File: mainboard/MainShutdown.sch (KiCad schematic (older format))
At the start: 41 parts, among them J5 AIR-, J6 AIR+, K1 KT12-1A, K2 UMS05-1A80-75L, Q1 TSM2306, Q14 BC846AW, Q17 DMN10H220L-7, Q18 TSM2306, Q19 TSM2306, Q20 TSM2306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

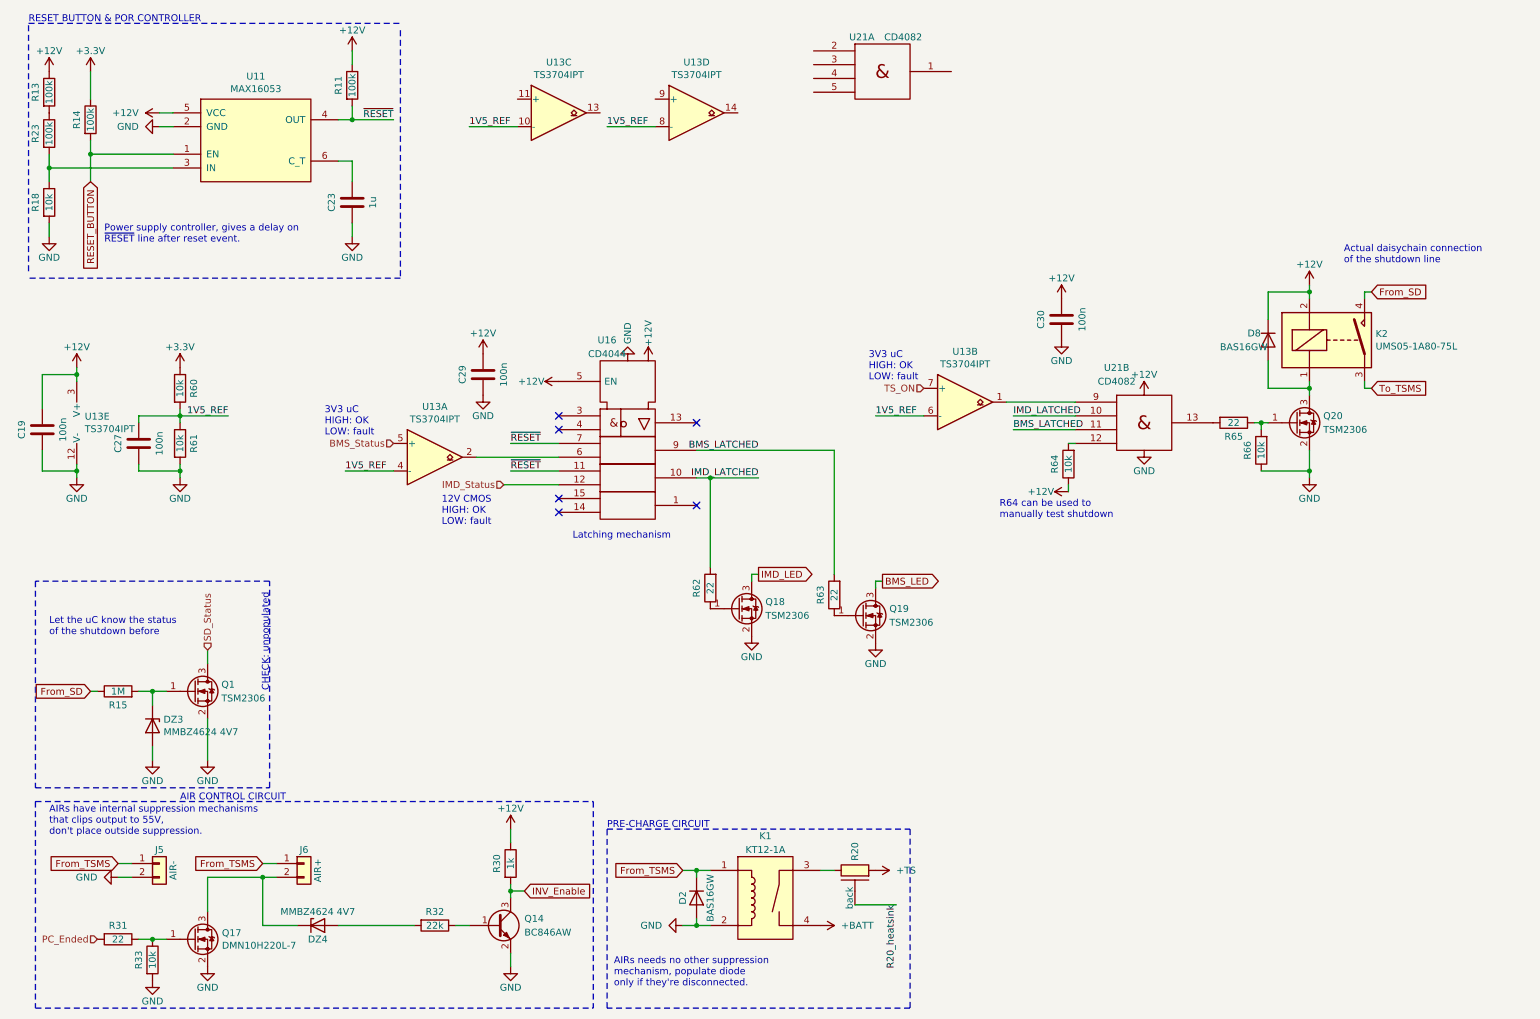
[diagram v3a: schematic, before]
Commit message: corrected pulldown and air+ mosfet driving
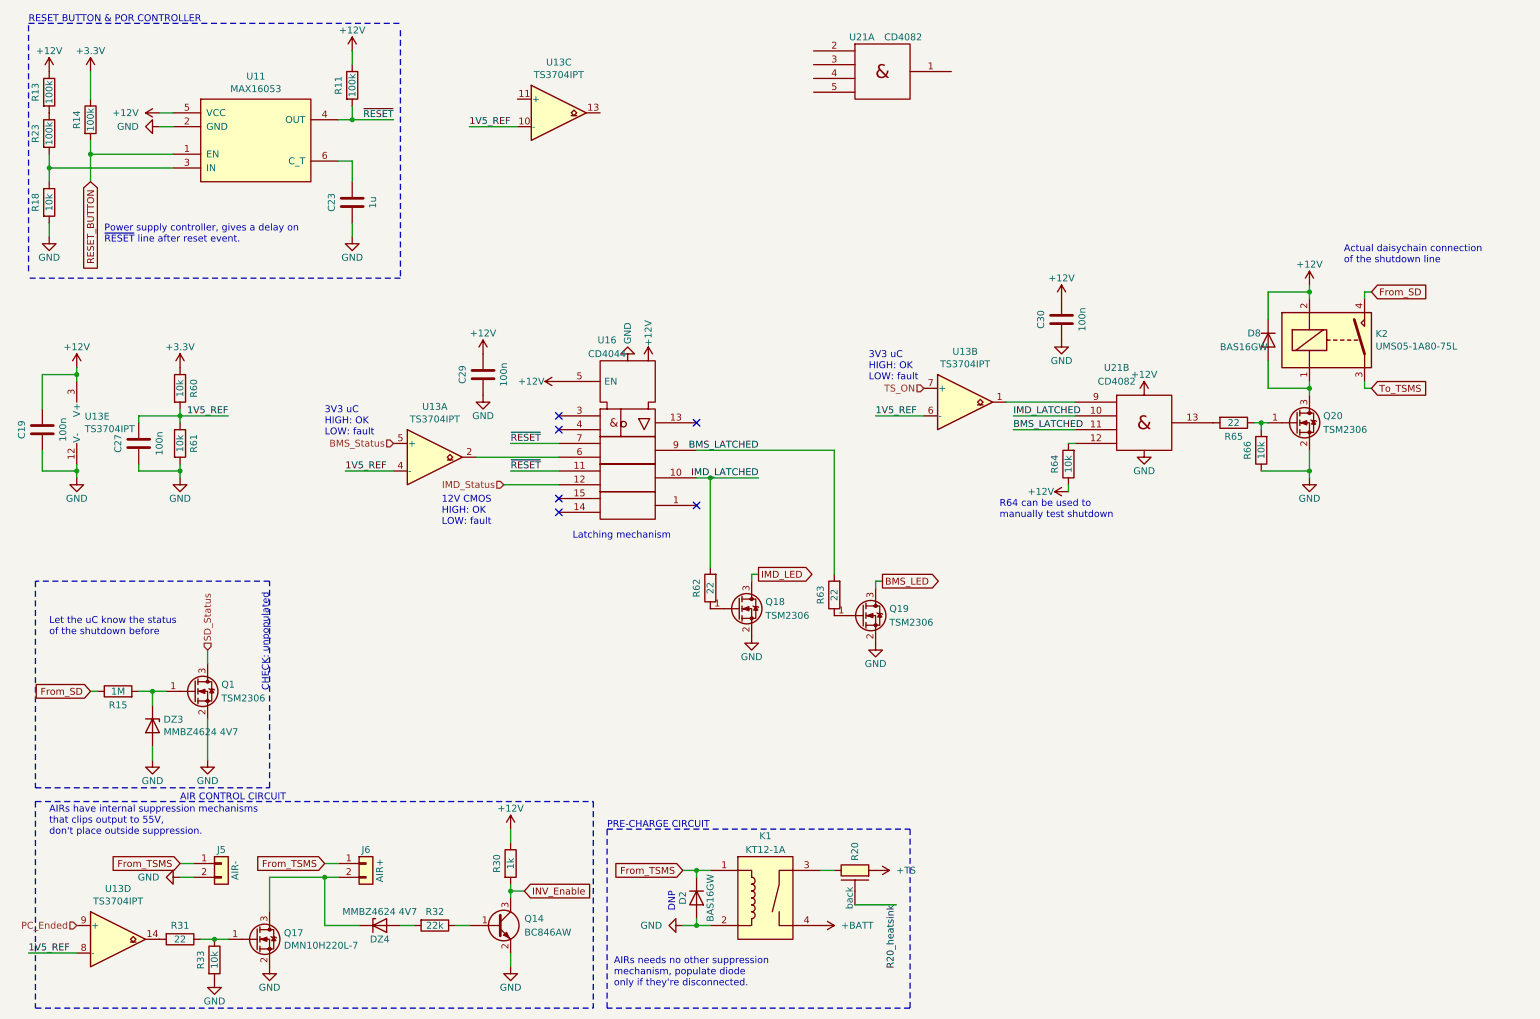
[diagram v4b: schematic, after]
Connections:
- net PC_Ended: now also U13.9 (+); no longer R31.2
- net at U13.14: now also R31.2
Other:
- note added: "DNP"
- moved on the sheet: DZ4, J5, J6, Q17, R31, R33, U13D
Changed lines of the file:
@@
 L Connector_Generic:Conn_01x02 J6
 U 1 1 5B0DE10C
-P 2550 6700
-F 0 "J6" H 2550 6800 50  0000 C CNN
-F 1 "AIR+" V 2650 6650 50  0000 C CNN
-F 2 "Connector_Molex:Molex_Micro-Fit_3.0_43650-0215_1x02_P3.00mm_Vertical" H 2550 6700 50  0001 C CNN
-F 3 "http://www.gigavac.com/sites/default/files/catalog/spec_sheet/gx14.pdf" H 2550 6700 50  0001 C CNN
-	1    2550 6700
+P 3000 6700
+F 0 "J6" H 3000 6800 50  0000 C CNN
+F 1 "AIR+" V 3100 6650 50  0000 C CNN
+F 2 "Connector_Molex:Molex_Micro-Fit_3.0_43650-0215_1x02_P3.00mm_Vertical" H 3000 6700 50  0001 C CNN
+F 3 "http://www.gigavac.com/sites/default/files/catalog/spec_sheet/gx14.pdf" H 3000 6700 50  0001 C CNN
+	1    3000 6700
 	1    0    0    -1
 $EndComp
@@
 L Device:R R33
 U 1 1 5B0DE119
-P 1450 7400
-F 0 "R33" V 1350 7400 50  0000 C CNN
-F 1 "10k" V 1450 7400 50  0000 C CNN
-F 2 "Resistor_SMD:R_0805_2012Metric" V 1380 7400 50  0001 C CNN
-F 3 "~" H 1450 7400 50  0001 C CNN
-	1    1450 7400
+P 1900 7400
+F 0 "R33" V 1800 7400 50  0000 C CNN
+F 1 "10k" V 1900 7400 50  0000 C CNN
+F 2 "Resistor_SMD:R_0805_2012Metric" V 1830 7400 50  0001 C CNN
+F 3 "~" H 1900 7400 50  0001 C CNN
+	1    1900 7400
 	1    0    0    -1
 $EndComp
@@
 L power:GND #PWR094
 U 1 1 5B0DE121
-P 1450 7550
-F 0 "#PWR094" H 1450 7300 50  0001 C CNN
-F 1 "GND" H 1450 7400 50  0000 C CNN
-F 2 "" H 1450 7550 50  0001 C CNN
-F 3 "" H 1450 7550 50  0001 C CNN
-	1    1450 7550
+P 1900 7550
+F 0 "#PWR094" H 1900 7300 50  0001 C CNN
+F 1 "GND" H 1900 7400 50  0000 C CNN
+F 2 "" H 1900 7550 50  0001 C CNN
+F 3 "" H 1900 7550 50  0001 C CNN
+	1    1900 7550
 	1    0    0    -1
 $EndComp
@@
 L Device:R R31
 U 1 1 5B0DE127
-P 1200 7250
-F 0 "R31" V 1100 7250 50  0000 C CNN
-F 1 "22" V 1200 7250 50  0000 C CNN
-F 2 "Resistor_SMD:R_0805_2012Metric" V 1130 7250 50  0001 C CNN
-F 3 "~" H 1200 7250 50  0001 C CNN
-	1    1200 7250
+P 1650 7250
+F 0 "R31" V 1550 7250 50  0000 C CNN
+F 1 "22" V 1650 7250 50  0000 C CNN
+F 2 "Resistor_SMD:R_0805_2012Metric" V 1580 7250 50  0001 C CNN
+F 3 "~" H 1650 7250 50  0001 C CNN
+	1    1650 7250
 	0    1    1    0
 $EndComp
@@
 L Device:D_Zener DZ4
 U 1 1 5B0DE15E
-P 2650 7150
-F 0 "DZ4" H 2650 7050 50  0000 C CNN
-F 1 "MMBZ4624 4V7" H 2650 7250 50  0000 C CNN
-F 2 "Diode_SMD:D_SOT-23_ANK" H 2650 7150 50  0001 C CNN
-F 3 "http://www.vishay.com/docs/85770/mmbz4617.pdf" H 2650 7150 50  0001 C CNN
-	1    2650 7150
+P 3100 7150
+F 0 "DZ4" H 3100 7050 50  0000 C CNN
+F 1 "MMBZ4624 4V7" H 3100 7250 50  0000 C CNN
+F 2 "Diode_SMD:D_SOT-23_ANK" H 3100 7150 50  0001 C CNN
+F 3 "http://www.vishay.com/docs/85770/mmbz4617.pdf" H 3100 7150 50  0001 C CNN
+	1    3100 7150
 	1    0    0    -1
 $EndComp
@@
 L Connector_Generic:Conn_01x02 J5
 U 1 1 5B0DE167
-P 1500 6700
-F 0 "J5" H 1500 6800 50  0000 C CNN
-F 1 "AIR-" V 1600 6650 50  0000 C CNN
-F 2 "Connector_Molex:Molex_Micro-Fit_3.0_43650-0215_1x02_P3.00mm_Vertical" H 1500 6700 50  0001 C CNN
-F 3 "http://www.gigavac.com/sites/default/files/catalog/spec_sheet/gx14.pdf" H 1500 6700 50  0001 C CNN
-	1    1500 6700
+P 1950 6700
+F 0 "J5" H 1950 6800 50  0000 C CNN
+F 1 "AIR-" V 2050 6650 50  0000 C CNN
+F 2 "Connector_Molex:Molex_Micro-Fit_3.0_43650-0215_1x02_P3.00mm_Vertical" H 1950 6700 50  0001 C CNN
+F 3 "http://www.gigavac.com/sites/default/files/catalog/spec_sheet/gx14.pdf" H 1950 6700 50  0001 C CNN
+	1    1950 6700
 	1    0    0    -1
 $EndComp
@@
 L power:GND #PWR091
 U 1 1 5B0DE170
-P 1200 6800
-F 0 "#PWR091" H 1200 6550 50  0001 C CNN
-F 1 "GND" V 1200 6650 50  0000 R CNN
-F 2 "" H 1200 6800 50  0001 C CNN
-F 3 "" H 1200 6800 50  0001 C CNN
-	1    1200 6800
+P 1650 6800
+F 0 "#PWR091" H 1650 6550 50  0001 C CNN
+F 1 "GND" V 1650 6650 50  0000 R CNN
+F 2 "" H 1650 6800 50  0001 C CNN
+F 3 "" H 1650 6800 50  0001 C CNN
+	1    1650 6800
 	0    1    1    0
 $EndComp
@@
 Wire Wire Line
 	5400 6750 5500 6750
-Text HLabel 1050 7250 0    50   Input ~ 0
+Text HLabel 900  7150 0    50   Input ~ 0
 PC_Ended
 Wire Wire Line
@@
 INV_Enable
 Wire Wire Line
-	2350 6700 2250 6700
-Text GLabel 2250 6700 0    50   Input ~ 0
+	2800 6700 2700 6700
+Text GLabel 2700 6700 0    50   Input ~ 0
 From_TSMS
 Wire Wire Line
-	1200 6800 1300 6800
-Wire Wire Line
-	1300 6700 1200 6700
-Text GLabel 1200 6700 0    50   Input ~ 0
+	1650 6800 1750 6800
+Wire Wire Line
+	1750 6700 1650 6700
+Text GLabel 1650 6700 0    50   Input ~ 0
 From_TSMS
 Wire Wire Line
@@
 L Device:Q_NMOS_GSD Q17
 U 1 1 6041C6DC
-P 1750 7250
-F 0 "Q17" H 1954 7296 50  0000 L CNN
-F 1 "DMN10H220L-7 " H 1954 7205 50  0000 L CNN
-F 2 "Package_TO_SOT_SMD:SOT-23" H 1950 7350 50  0001 C CNN
-F 3 "https://www.mouser.it/datasheet/2/196/irlml0100pbf-1228126.pdf" H 1750 7250 50  0001 C CNN
-	1    1750 7250
+P 2200 7250
+F 0 "Q17" H 2404 7296 50  0000 L CNN
+F 1 "DMN10H220L-7 " H 2404 7205 50  0000 L CNN
+F 2 "Package_TO_SOT_SMD:SOT-23" H 2400 7350 50  0001 C CNN
+F 3 "https://www.mouser.it/datasheet/2/196/irlml0100pbf-1228126.pdf" H 2200 7250 50  0001 C CNN
+	1    2200 7250
 	1    0    0    -1
 $EndComp
@@
 L power:GND #PWR0142
 U 1 1 604431DD
-P 1850 7450
-F 0 "#PWR0142" H 1850 7200 50  0001 C CNN
-F 1 "GND" H 1850 7300 50  0000 C CNN
-F 2 "" H 1850 7450 50  0001 C CNN
-F 3 "" H 1850 7450 50  0001 C CNN
-	1    1850 7450
-	1    0    0    -1
-$EndComp
-Connection ~ 1450 7250
-Wire Wire Line
-	1450 7250 1550 7250
-Wire Wire Line
-	1350 7250 1450 7250
+P 2300 7450
+F 0 "#PWR0142" H 2300 7200 50  0001 C CNN
+F 1 "GND" H 2300 7300 50  0000 C CNN
+F 2 "" H 2300 7450 50  0001 C CNN
+F 3 "" H 2300 7450 50  0001 C CNN
+	1    2300 7450
+	1    0    0    -1
+$EndComp
+Connection ~ 1900 7250
+Wire Wire Line
+	1900 7250 2000 7250
+Wire Wire Line
+	1800 7250 1900 7250
 Wire Wire Line
 	4400 3850 4050 3850
@@
 L Comparator:LM339 U13
 U 4 1 604EB5FB
-P 5400 1250
-F 0 "U13" H 5400 1617 50  0000 C CNN
-F 1 "TS3704IPT" H 5400 1526 50  0000 C CNN
-F 2 "Package_SO:TSSOP-14_4.4x5mm_P0.65mm" H 5350 1350 50  0001 C CNN
-F 3 "https://www.st.com/resource/en/datasheet/lm139.pdf" H 5450 1450 50  0001 C CNN
-	4    5400 1250
+P 1200 7250
+F 0 "U13" H 1200 7617 50  0000 C CNN
+F 1 "TS3704IPT" H 1200 7526 50  0000 C CNN
+F 2 "Package_SO:TSSOP-14_4.4x5mm_P0.65mm" H 1150 7350 50  0001 C CNN
+F 3 "https://www.st.com/resource/en/datasheet/lm139.pdf" H 1250 7450 50  0001 C CNN
+	4    1200 7250
 	1    0    0    -1
 $EndComp
@@
 Wire Wire Line
 	3750 1350 4100 1350
-Text Label 4750 1350 0    50   ~ 0
+Text Label 550  7350 0    50   ~ 0
 1V5_REF
 Wire Wire Line
-	4750 1350 5100 1350
+	550  7350 900  7350
 Wire Wire Line
 	3800 3750 4400 3750
@@
 	600  6250 4650 6250
 Wire Wire Line
-	1850 7050 1850 6800
-Wire Wire Line
-	1850 6800 2250 6800
-Wire Wire Line
-	2500 7150 2250 7150
-Wire Wire Line
-	2250 7150 2250 6800
-Connection ~ 2250 6800
-Wire Wire Line
-	2250 6800 2350 6800
-Wire Wire Line
-	2800 7150 3350 7150
+	2300 7050 2300 6800
+Wire Wire Line
+	2300 6800 2700 6800
+Wire Wire Line
+	2950 7150 2700 7150
+Wire Wire Line
+	2700 7150 2700 6800
+Connection ~ 2700 6800
+Wire Wire Line
+	2700 6800 2800 6800
+Wire Wire Line
+	3250 7150 3350 7150
 $Comp
 L Comparator:LM339 U13
@@
 	700  1550 700  1650
 Connection ~ 700  1650
+Text Notes 5250 7050 1    50   ~ 0
+DNP
 $EndSCHEMATC
